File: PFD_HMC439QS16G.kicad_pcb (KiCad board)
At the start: 2 copper layers, 160 x 100 mm, 74 parts, among them J1 REF, J2 IN, J3 Error_Out, J4 C64AC, J5 Fast_Out, U1 HMC439QS16G, U2 LT3045EMSE, U3 LT3094EMSE, U4 ADA4896-2ARMZ, U5 ADA4896-2ARMZ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

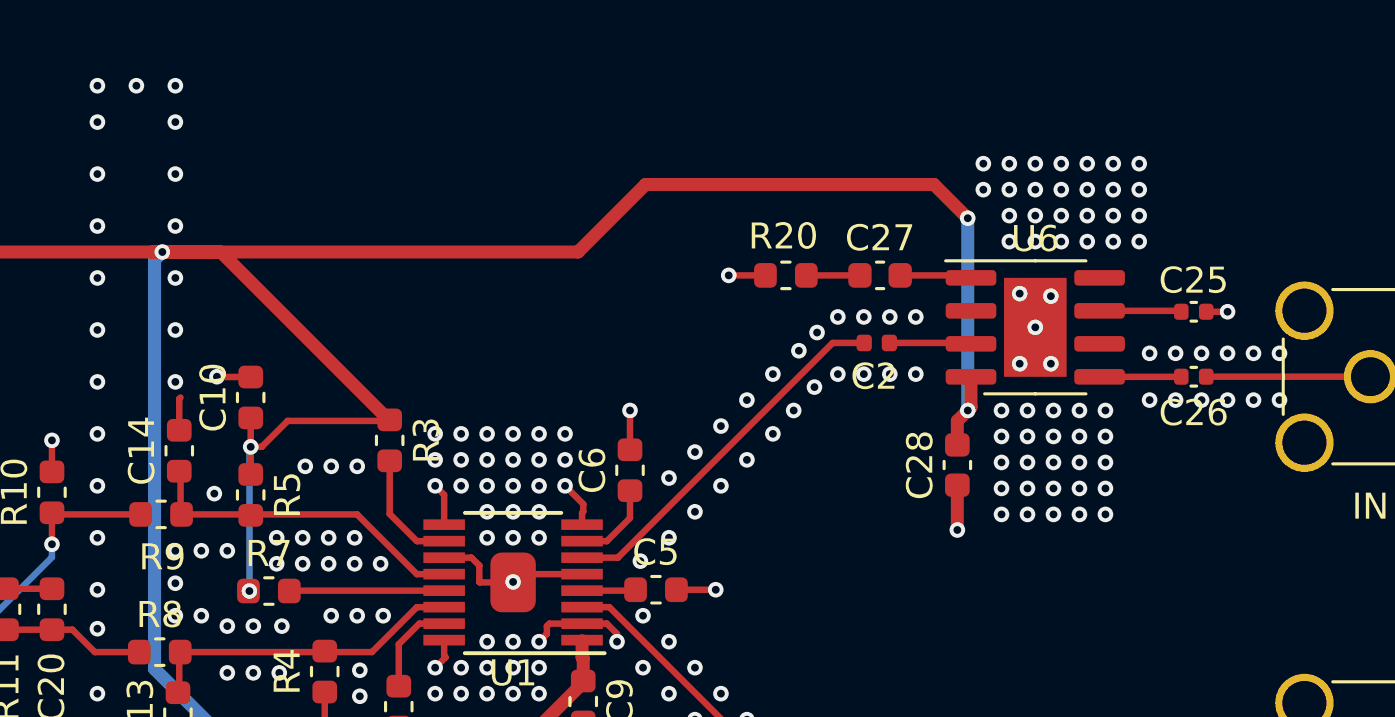
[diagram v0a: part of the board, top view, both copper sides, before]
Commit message: Remove HMC365 frequency divider
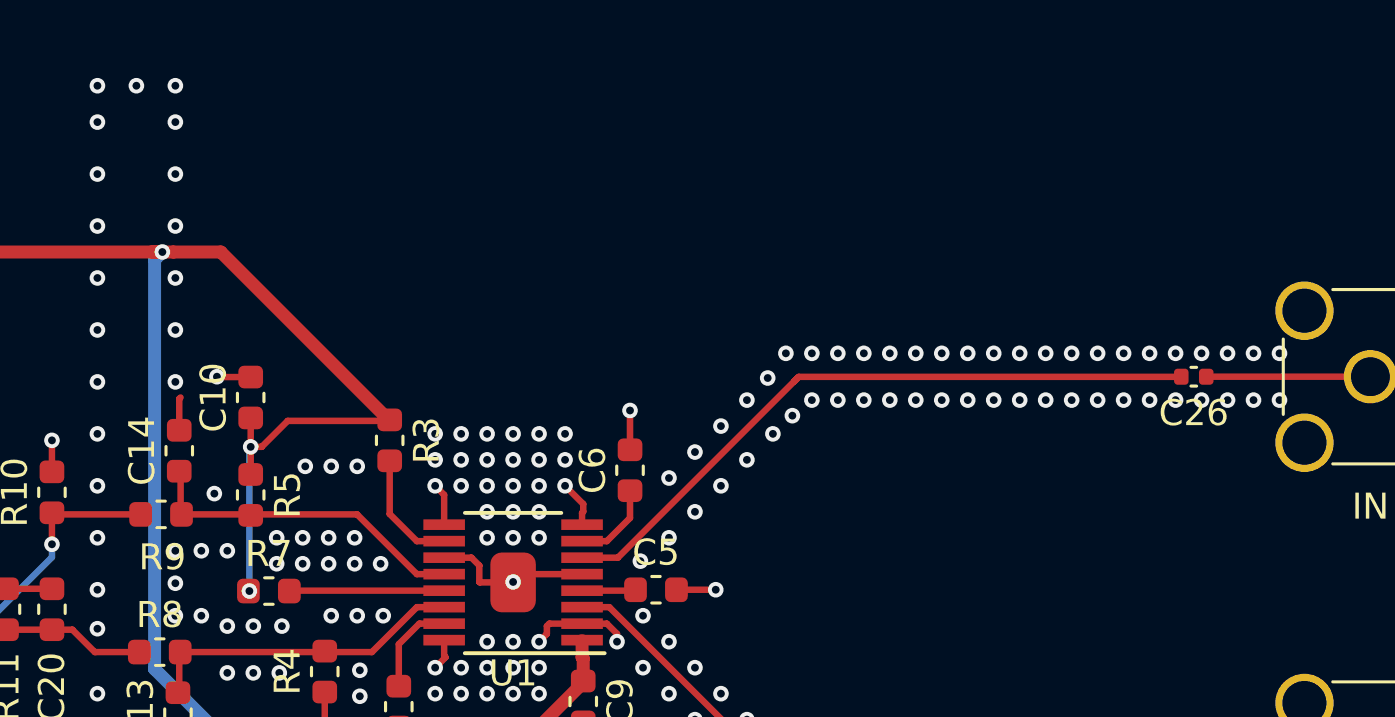
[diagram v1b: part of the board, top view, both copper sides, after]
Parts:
- removed C2, C25: 100p, Capacitor_SMD:C_0402_1005Metric
- removed C27: 1n, Capacitor_SMD:C_0603_1608Metric
- removed C28: 100n, Capacitor_SMD:C_0603_1608Metric
- removed R20: 49.9, Resistor_SMD:R_0603_1608Metric
- removed U6: HMC365S8G, Package_SO:SOIC-8-1EP_3.9x4.9mm_P1.27mm_EP2.41x3.81mm
- C20: value 560p -> 15p
- R10, R11: value 200 -> 380
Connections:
- U1 pad 6: Net-(C2-Pad1) -> Net-(C26-Pad1)
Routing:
- net +5V: track 326.4 -> 283.6 mm, vias 10 -> 8
- net Net-(C26-Pad1): track 3.15 -> 26.1 mm
- net Net-(C2-Pad1): track 14.3 -> 0.00 mm
- net GND: track 85.6 -> 74.6 mm, vias 339 -> 296
- net Div_out: track 3.17 -> 0.00 mm
- net Net-(C25-Pad2): track 3.16 -> 0.00 mm
- net Net-(C27-Pad2): track 2.76 -> 0.00 mm
- net Net-(C27-Pad1): track 2.06 -> 0.00 mm

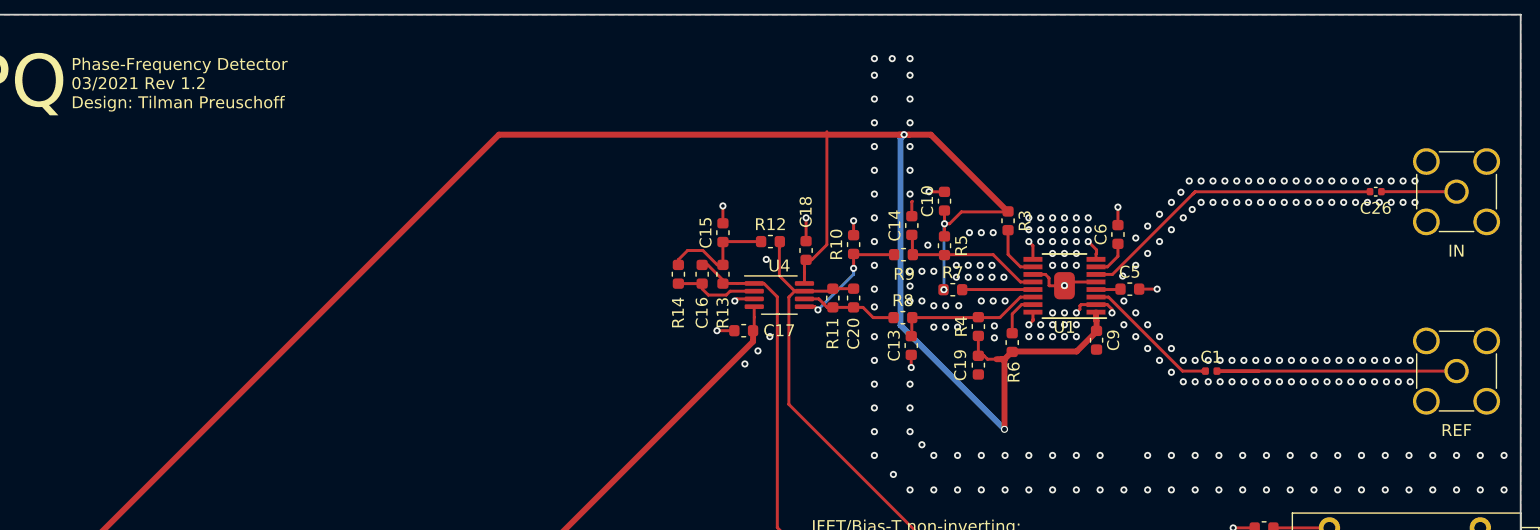
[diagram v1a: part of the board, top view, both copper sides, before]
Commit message: Update revision label on PCB
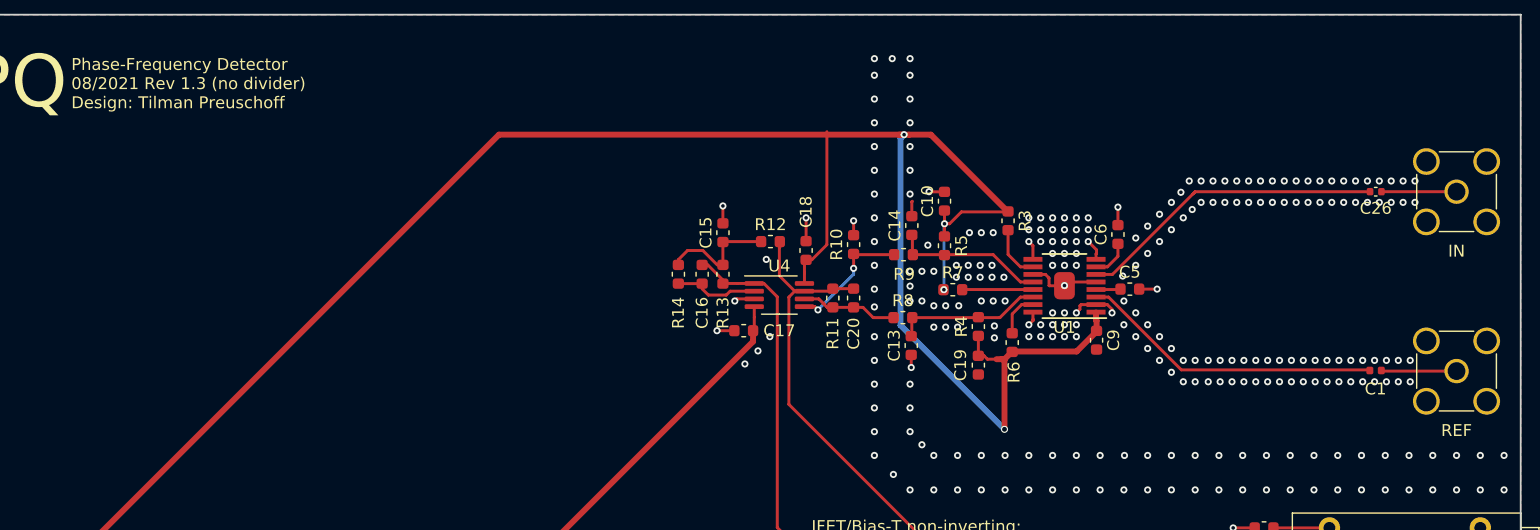
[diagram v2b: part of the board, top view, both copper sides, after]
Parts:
- moved C1 13.8 mm to (217.8, 80.0)
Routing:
- net Net-(C1-Pad2): track 24.6 -> 6.35 mm
- net Net-(C1-Pad1): track 11.8 -> 25.6 mm
- net GND: vias 296 -> 297
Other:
- board text added: "Phase-Frequency Detector 08/2021 Rev 1.3 (no divider) Design: Tilman Preuschoff"
- board text removed: "Phase-Frequency Detector 03/2021 Rev 1.2 Design: Tilman Preuschoff"

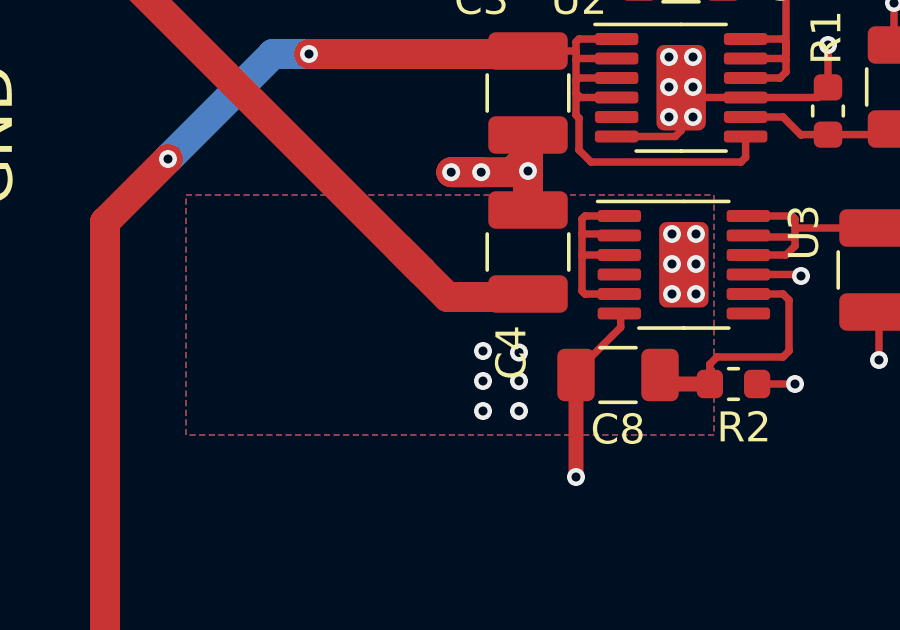
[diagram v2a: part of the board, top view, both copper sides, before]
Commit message: Update error signal gains and fix copper pour at LT3094
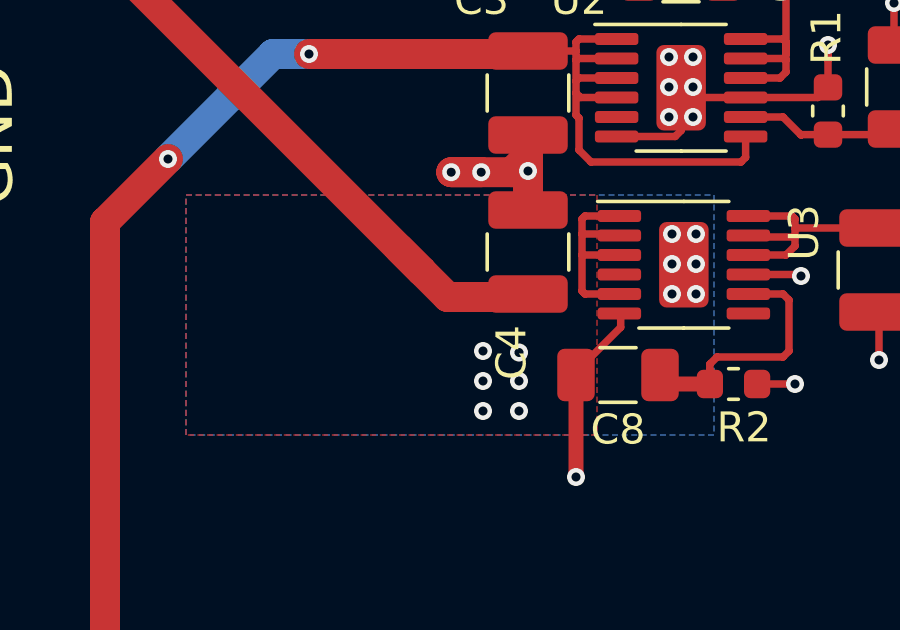
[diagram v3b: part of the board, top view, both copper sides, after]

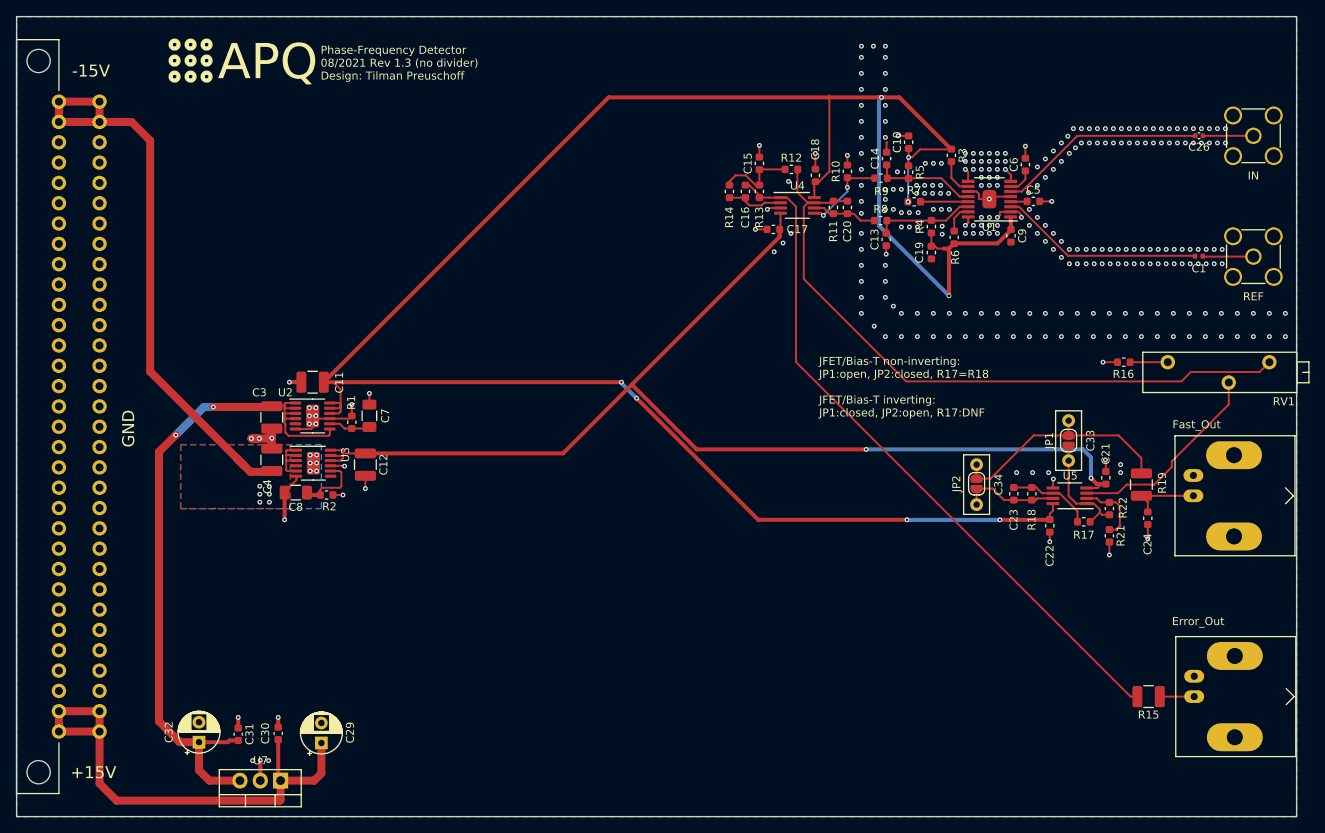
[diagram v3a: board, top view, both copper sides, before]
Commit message: Add LM7908 and TVS diodes for line protection
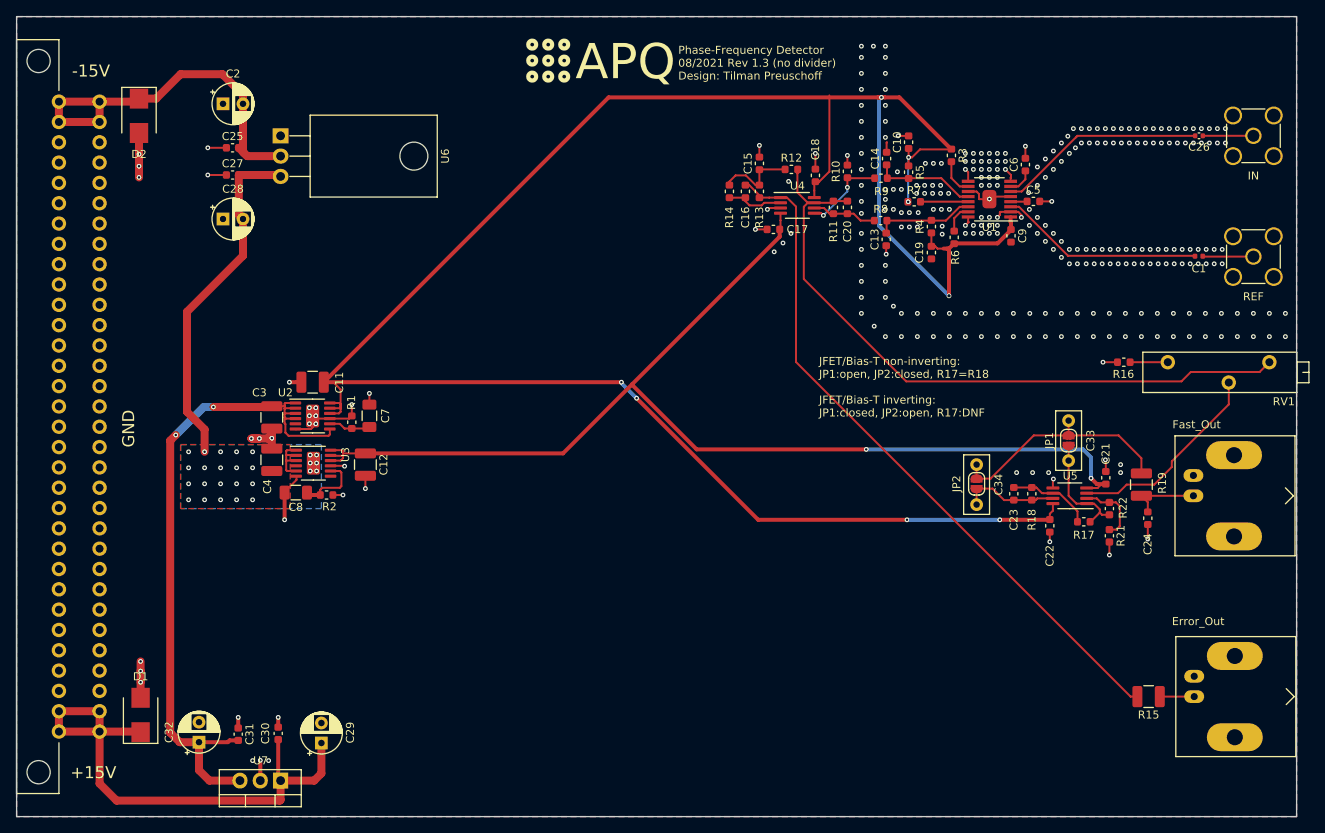
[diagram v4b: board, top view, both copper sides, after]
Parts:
- added C2: 100u, Capacitor_THT:CP_Radial_D5.0mm_P2.50mm, F.Cu at (95.8, 60.9)
- added C25: 100n, Capacitor_SMD:C_0603_1608Metric, F.Cu at (97.0, 66.4)
- added C27: 100n, Capacitor_SMD:C_0603_1608Metric, F.Cu at (97.0, 69.8)
- added C28: 100u, Capacitor_THT:CP_Radial_D5.0mm_P2.50mm, F.Cu at (95.8, 75.3)
- added D1: SMB, Diode_SMD:D_SMB, F.Cu at (85.5, 137.3)
- added D2: SMB, Diode_SMD:D_SMB, F.Cu at (85.3, 62.4)
- added U6: LM7908_TO220, Package_TO_SOT_THT:TO-220-3_Horizontal_TabDown, F.Cu at (103.0, 64.9)
- C16: value 140p -> 150p
- C7, C8: value 0.47u -> 100n C0G
- U7: value L7809 -> LM7808
- moved LOGO1 44.7 mm to (134.2, 53.0)
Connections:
- C4 pad 1: IN -> -9V
- J4 pad A31: IN -> -15V
- J4 pad A32: IN -> -15V
- J4 pad C31: IN -> -15V
- J4 pad C32: IN -> -15V
- U3 pad 1: IN -> -9V
- U3 pad 13: IN -> -9V
- U3 pad 2: IN -> -9V
- U3 pad 3: IN -> -9V
- U3 pad 5: IN -> -9V
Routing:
- net IN: track 80.4 -> 0.00 mm, vias 12 -> 0
- net -9V: track 0.00 -> 51.4 mm, vias 0 -> 26
- net -15V: track 0.00 -> 48.8 mm
- net GND: track 74.6 -> 89.3 mm, vias 297 -> 305
- net +15V: track 62.2 -> 67.4 mm
- net +9V: track 88.0 -> 86.8 mm
- added copper zone on B.Cu, net -9V
- added copper zone on F.Cu, net -9V
- removed copper zone on B.Cu, net IN
- removed copper zone on F.Cu, net IN
